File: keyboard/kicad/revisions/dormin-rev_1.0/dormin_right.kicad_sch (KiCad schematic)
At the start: 113 parts, among them J4_R1 Conn_01x06, J4_R2 Conn_01x02, J6_R1 Conn_01x04, Q3_R1 AO3407A, Q4_R1 AO3400A, SW21 SW_Push, SW22 SW_Push, SW23 SW_Push, SW24 SW_Push, SW25 SW_Push, SW26 SW_Push, SW27 SW_Push, SW28 SW_Push, SW29 SW_Push, SW30 SW_Push, SW31 SW_Push, SW32 SW_Push, SW33 SW_Push, SW34 SW_Push, SW35 SW_Push, SW36 SW_Push, SW37 SW_Push, SW38 SW_Push, SW39 SW_Push, SW40 SW_Push, U5_R1 XIAO-nRF52840-Plus-SMD

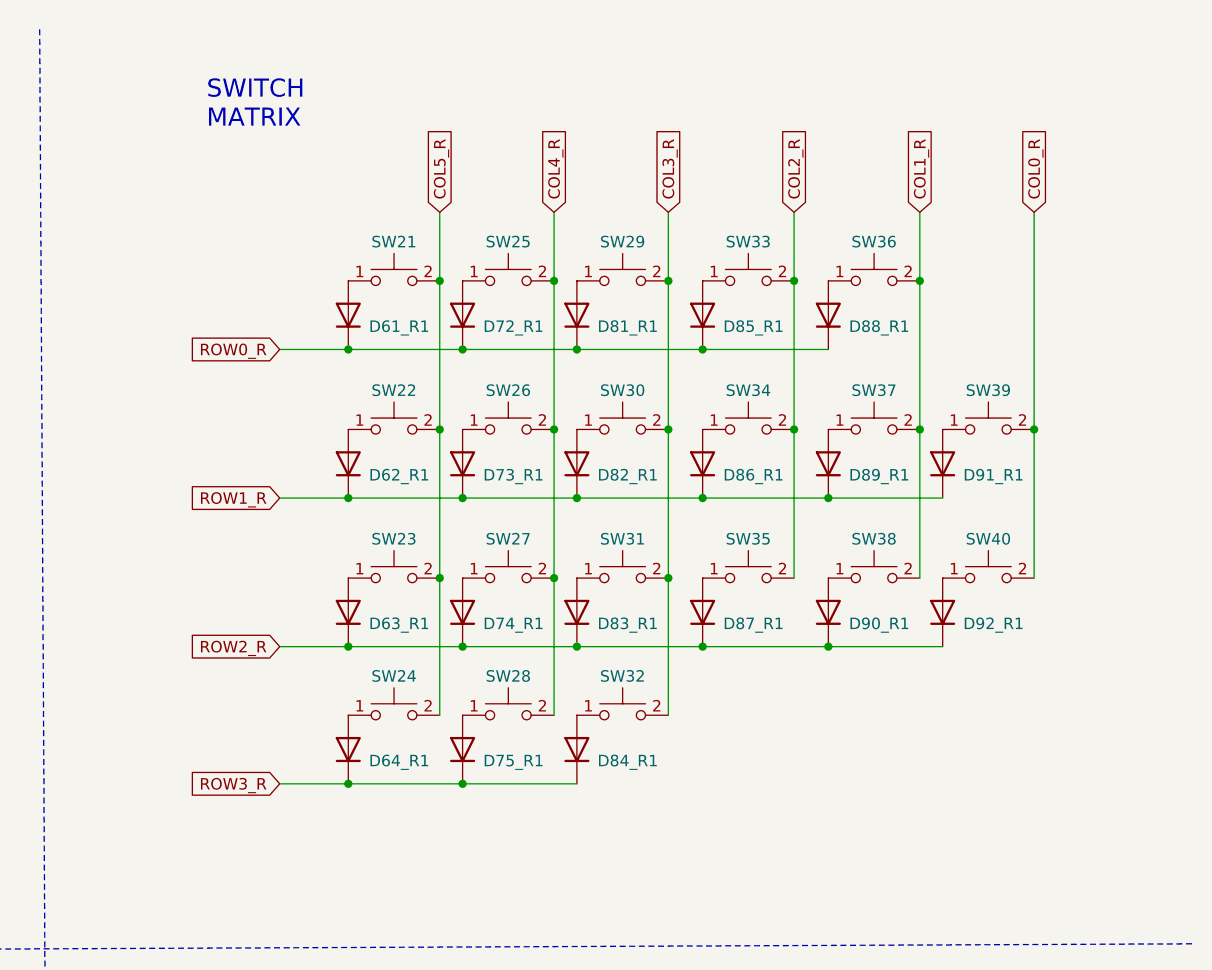
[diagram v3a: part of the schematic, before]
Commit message: feat: adjust schematics for the switches logic order
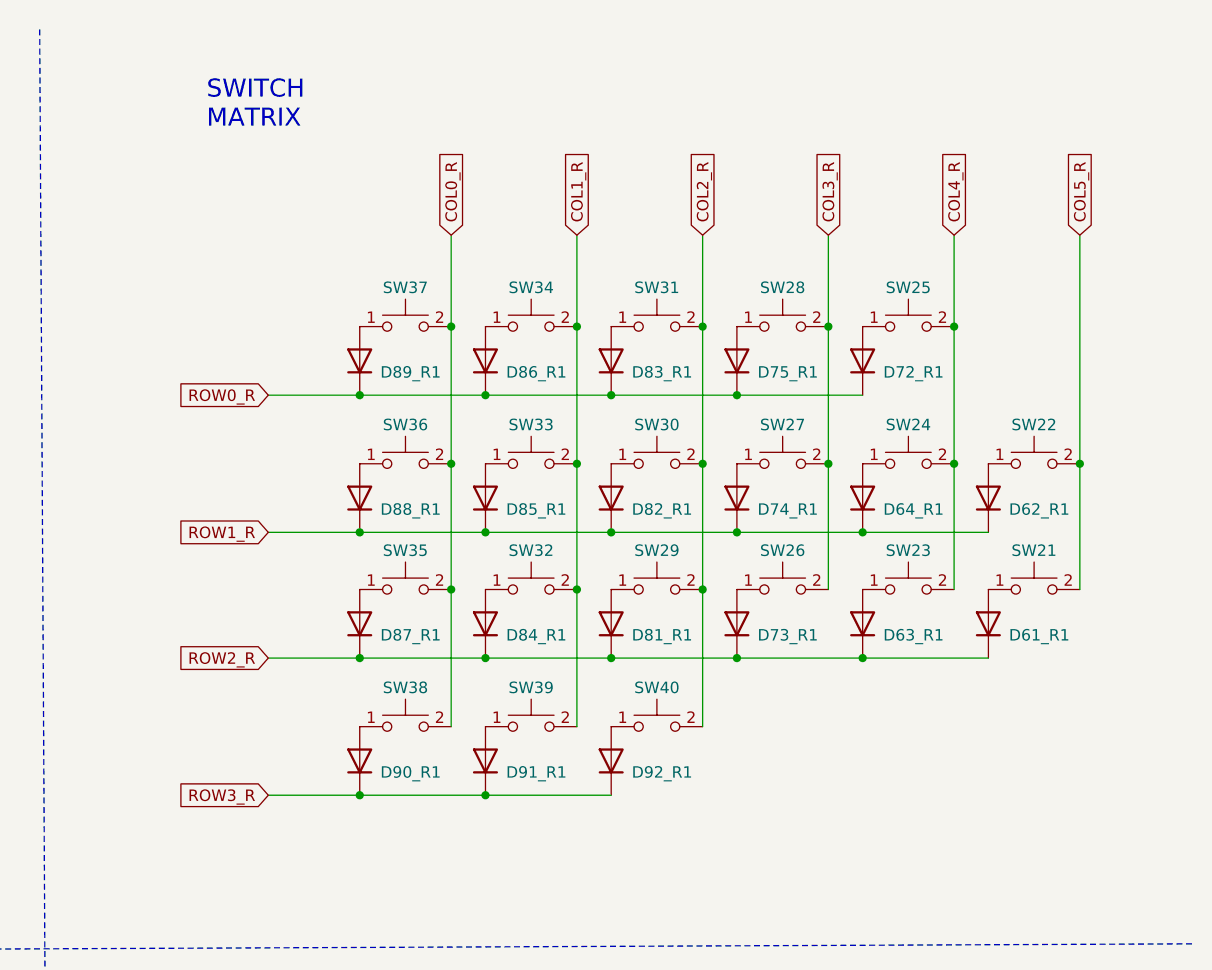
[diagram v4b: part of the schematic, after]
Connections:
- net COL0_R: now also SW35.2, SW36.2, SW37.2, SW38.2; no longer SW39.2, SW40.2
- net COL1_R: now also SW32.2, SW33.2, SW34.2, SW39.2; no longer SW36.2, SW37.2, SW38.2
- net COL2_R: now also SW29.2, SW30.2, SW31.2, SW40.2; no longer SW33.2, SW34.2, SW35.2
- net COL3_R: now also SW26.2, SW27.2, SW28.2; no longer SW29.2, SW30.2, SW31.2, SW32.2
- net COL4_R: now also SW23.2, SW24.2; no longer SW26.2, SW27.2, SW28.2
- net COL5_R: no longer SW23.2, SW24.2
- net ROW0_R: now also D75_R1.1 (K), D83_R1.1 (K), D86_R1.1 (K), D89_R1.1 (K); no longer D61_R1.1 (K), D81_R1.1 (K), D85_R1.1 (K), D88_R1.1 (K)
- net ROW1_R: now also D64_R1.1 (K), D74_R1.1 (K), D85_R1.1 (K), D88_R1.1 (K); no longer D73_R1.1 (K), D86_R1.1 (K), D89_R1.1 (K), D91_R1.1 (K)
- net ROW2_R: now also D61_R1.1 (K), D73_R1.1 (K), D81_R1.1 (K), D84_R1.1 (K); no longer D74_R1.1 (K), D83_R1.1 (K), D90_R1.1 (K), D92_R1.1 (K)
- net ROW3_R: now also D90_R1.1 (K), D91_R1.1 (K), D92_R1.1 (K); no longer D64_R1.1 (K), D75_R1.1 (K), D84_R1.1 (K)
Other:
- moved on the sheet: D61_R1, D62_R1, D63_R1, D64_R1, D72_R1, D73_R1, D74_R1, D75_R1, D81_R1, D82_R1, D83_R1, D84_R1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

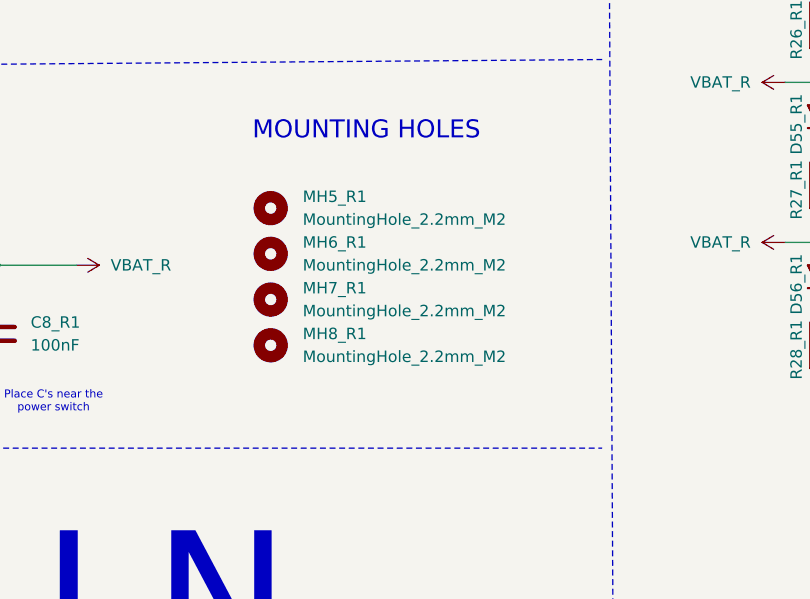
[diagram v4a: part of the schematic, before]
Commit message: feat: added routing to the left pcb
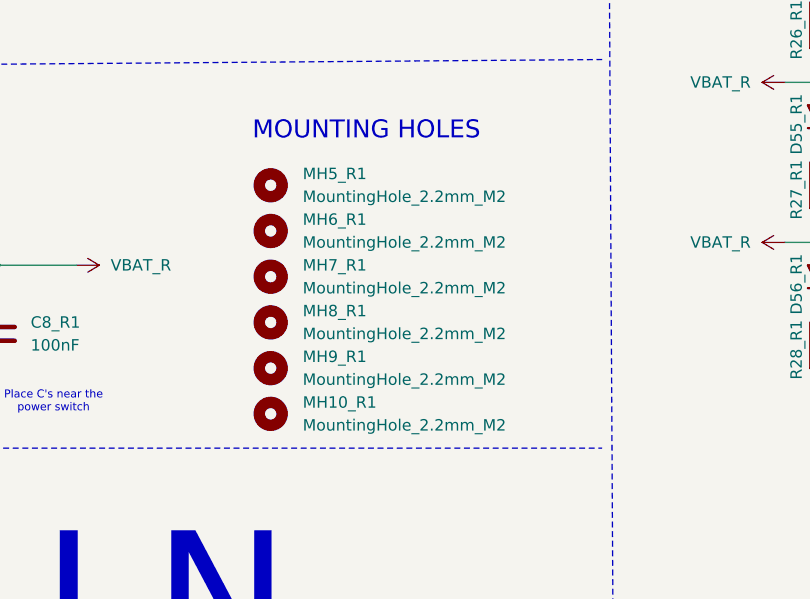
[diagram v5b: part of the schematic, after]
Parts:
- added MH10_R1, MH9_R1: MountingHole_2.2mm_M2, MountingHole:MountingHole_2.2mm_M2, symbol Mechanical:MountingHole
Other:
- moved on the sheet: MH5_R1, MH6_R1, MH7_R1, MH8_R1
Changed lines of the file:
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@@
 	(symbol
 		(lib_id "Mechanical:MountingHole")
-		(at 139.7 187.96 0)
+		(at 139.7 185.42 0)
 		(unit 1)
 		(body_style 1)
@@
 		(dnp no)
 		(property "Reference" "MH6_R1"
-			(at 143.256 186.6899 0)
+			(at 143.256 184.1499 0)
 			(show_name no)
 			(do_not_autoplace no)
@@
 		)
 		(property "Value" "MountingHole_2.2mm_M2"
-			(at 143.256 189.2299 0)
+			(at 143.256 186.6899 0)
 			(show_name no)
 			(do_not_autoplace no)
@@
 		)
 		(property "Footprint" "MountingHole:MountingHole_2.2mm_M2"
-			(at 139.7 187.96 0)
+			(at 139.7 185.42 0)
 			(hide yes)
 			(show_name no)
@@
 		)
 		(property "Datasheet" ""
-			(at 139.7 187.96 0)
+			(at 139.7 185.42 0)
 			(hide yes)
 			(show_name no)
@@
 		)
 		(property "Description" ""
-			(at 139.7 187.96 0)
+			(at 139.7 185.42 0)
 			(hide yes)
 			(show_name no)
@@
 	(symbol
 		(lib_id "Mechanical:MountingHole")
-		(at 139.7 198.12 0)
+		(at 139.7 195.58 0)
 		(unit 1)
 		(body_style 1)
@@
 		(dnp no)
 		(property "Reference" "MH8_R1"
-			(at 143.256 196.8499 0)
+			(at 143.256 194.3099 0)
 			(show_name no)
 			(do_not_autoplace no)
@@
 		)
 		(property "Value" "MountingHole_2.2mm_M2"
-			(at 143.256 199.3899 0)
+			(at 143.256 196.8499 0)
 			(show_name no)
 			(do_not_autoplace no)
@@
 		)
 		(property "Footprint" "MountingHole:MountingHole_2.2mm_M2"
-			(at 139.7 198.12 0)
+			(at 139.7 195.58 0)
 			(hide yes)
 			(show_name no)
@@
 		)
 		(property "Datasheet" ""
-			(at 139.7 198.12 0)
+			(at 139.7 195.58 0)
 			(hide yes)
 			(show_name no)
@@
 		)
 		(property "Description" ""
-			(at 139.7 198.12 0)
+			(at 139.7 195.58 0)
 			(hide yes)
 			(show_name no)
@@
 	(symbol
 		(lib_id "Mechanical:MountingHole")
-		(at 139.7 182.88 0)
+		(at 139.7 180.34 0)
 		(unit 1)
 		(body_style 1)
@@
 		(dnp no)
 		(property "Reference" "MH5_R1"
-			(at 143.256 181.6099 0)
+			(at 143.256 179.0699 0)
 			(show_name no)
 			(do_not_autoplace no)
@@
 		)
 		(property "Value" "MountingHole_2.2mm_M2"
-			(at 143.256 184.1499 0)
+			(at 143.256 181.6099 0)
 			(show_name no)
 			(do_not_autoplace no)
@@
 		)
 		(property "Footprint" "MountingHole:MountingHole_2.2mm_M2"
-			(at 139.7 182.88 0)
+			(at 139.7 180.34 0)
 			(hide yes)
 			(show_name no)
@@
 		)
 		(property "Datasheet" ""
-			(at 139.7 182.88 0)
+			(at 139.7 180.34 0)
 			(hide yes)
 			(show_name no)
@@
 		)
 		(property "Description" ""
-			(at 139.7 182.88 0)
+			(at 139.7 180.34 0)
 			(hide yes)
 			(show_name no)
@@
 	)
 	(symbol
+		(lib_id "Mechanical:MountingHole")
+		(at 139.7 200.66 0)
+		(unit 1)
+		(body_style 1)
+		(exclude_from_sim no)
+		(in_bom yes)
+		(on_board yes)
+		(in_pos_files yes)
+		(dnp no)
+		(property "Reference" "MH9_R1"
+			(at 143.256 199.3899 0)
+			(show_name no)
+			(do_not_autoplace no)
+			(effects
+				(font
+					(size 1.27 1.27)
+				)
+				(justify left)
+			)
+		)
+		(property "Value" "MountingHole_2.2mm_M2"
+			(at 143.256 201.9299 0)
+			(show_name no)
+			(do_not_autoplace no)
+			(effects
+				(font
+					(size 1.27 1.27)
+				)
+				(justify left)
+			)
+		)
+		(property "Footprint" "MountingHole:MountingHole_2.2mm_M2"
+			(at 139.7 200.66 0)
+			(hide yes)
+			(show_name no)
+			(do_not_autoplace no)
+			(effects
+				(font
+					(size 1.27 1.27)
+				)
+			)
+		)
+		(property "Datasheet" ""
+			(at 139.7 200.66 0)
+			(hide yes)
+			(show_name no)
+			(do_not_autoplace no)
+			(effects
+				(font
+					(size 1.27 1.27)
+				)
+			)
+		)
+		(property "Description" ""
+			(at 139.7 200.66 0)
+			(hide yes)
+			(show_name no)
+			(do_not_autoplace no)
+			(effects
+				(font
+					(size 1.27 1.27)
+				)
+			)
+		)
+		(instances
+			(project "dormin"
+				(path "/603afaa0-4142-4673-b835-76ba767ab9eb/c34ad971-40ee-4ba1-b588-4be495453fb3"
+					(reference "MH9_R1")
+					(unit 1)
+				)
+			)
+		)
+	)
+	(symbol
 		(lib_id "Diode:1N4148W")
 		(at 240.03 50.8 90)
@@
 	(symbol
 		(lib_id "Mechanical:MountingHole")
-		(at 139.7 193.04 0)
+		(at 139.7 190.5 0)
 		(unit 1)
 		(body_style 1)
@@
 		(dnp no)
 		(property "Reference" "MH7_R1"
-			(at 143.256 191.7699 0)
+			(at 143.256 189.2299 0)
 			(show_name no)
 			(do_not_autoplace no)
@@
 		)
 		(property "Value" "MountingHole_2.2mm_M2"
-			(at 143.256 194.3099 0)
+			(at 143.256 191.7699 0)
 			(show_name no)
 			(do_not_autoplace no)
@@
 		)
 		(property "Footprint" "MountingHole:MountingHole_2.2mm_M2"
-			(at 139.7 193.04 0)
+			(at 139.7 190.5 0)
 			(hide yes)
 			(show_name no)
@@
 		)
 		(property "Datasheet" ""
-			(at 139.7 193.04 0)
+			(at 139.7 190.5 0)
 			(hide yes)
 			(show_name no)
@@
 		)
 		(property "Description" ""
-			(at 139.7 193.04 0)
+			(at 139.7 190.5 0)
 			(hide yes)
 			(show_name no)
@@
 					(unit 1)
 				)
+			)
+		)
+	)
+	(symbol
+		(lib_id "Mechanical:MountingHole")
+		(at 139.7 205.74 0)
+		(unit 1)
+		(body_style 1)
+		(exclude_from_sim no)
+		(in_bom yes)
+		(on_board yes)
+		(in_pos_files yes)
+		(dnp no)
+		(property "Reference" "MH10_R1"
+			(at 143.256 204.4699 0)
+			(show_name no)
+			(do_not_autoplace no)
+			(effects
+				(font
+					(size 1.27 1.27)
+				)
+				(justify left)
+			)
+		)
+		(property "Value" "MountingHole_2.2mm_M2"
+			(at 143.256 207.0099 0)
+			(show_name no)
+			(do_not_autoplace no)
+			(effects
+				(font
+					(size 1.27 1.27)
+				)
+				(justify left)
+			)
+		)
+		(property "Footprint" "MountingHole:MountingHole_2.2mm_M2"
+			(at 139.7 205.74 0)
+			(hide yes)
+			(show_name no)
+			(do_not_autoplace no)
+			(effects
+				(font
+					(size 1.27 1.27)
+				)
+			)
+		)
+		(property "Datasheet" ""
+			(at 139.7 205.74 0)
+			(hide yes)
+			(show_name no)
+			(do_not_autoplace no)
+			(effects
+				(font
+					(size 1.27 1.27)
+				)
+			)
+		)
+		(property "Description" ""
+			(at 139.7 205.74 0)
+			(hide yes)
+			(show_name no)
+			(do_not_autoplace no)
+			(effects
+				(font
+					(size 1.27 1.27)
+				)
+			)
+		)
+		(instances
+			(project "dormin"
+				(path "/603afaa0-4142-4673-b835-76ba767ab9eb/c34ad971-40ee-4ba1-b588-4be495453fb3"
+					(reference "MH10_R1")
+					(unit 1)
+				)

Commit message: feat: added new pcb design
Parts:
- J4_R2: footprint willkeebs_misc:SMD_Conn_1x02_P2.54mm_Vertical -> willkeebs_components:Pogo1x2-Right-Angle
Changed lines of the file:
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@@
 			)
 		)
-		(property "Footprint" "willkeebs_misc:SMD_Conn_1x02_P2.54mm_Vertical"
+		(property "Footprint" "willkeebs_components:Pogo1x2-Right-Angle"
 			(at 135.89 43.18 0)
 			(hide yes)
